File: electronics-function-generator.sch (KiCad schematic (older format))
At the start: 23 parts

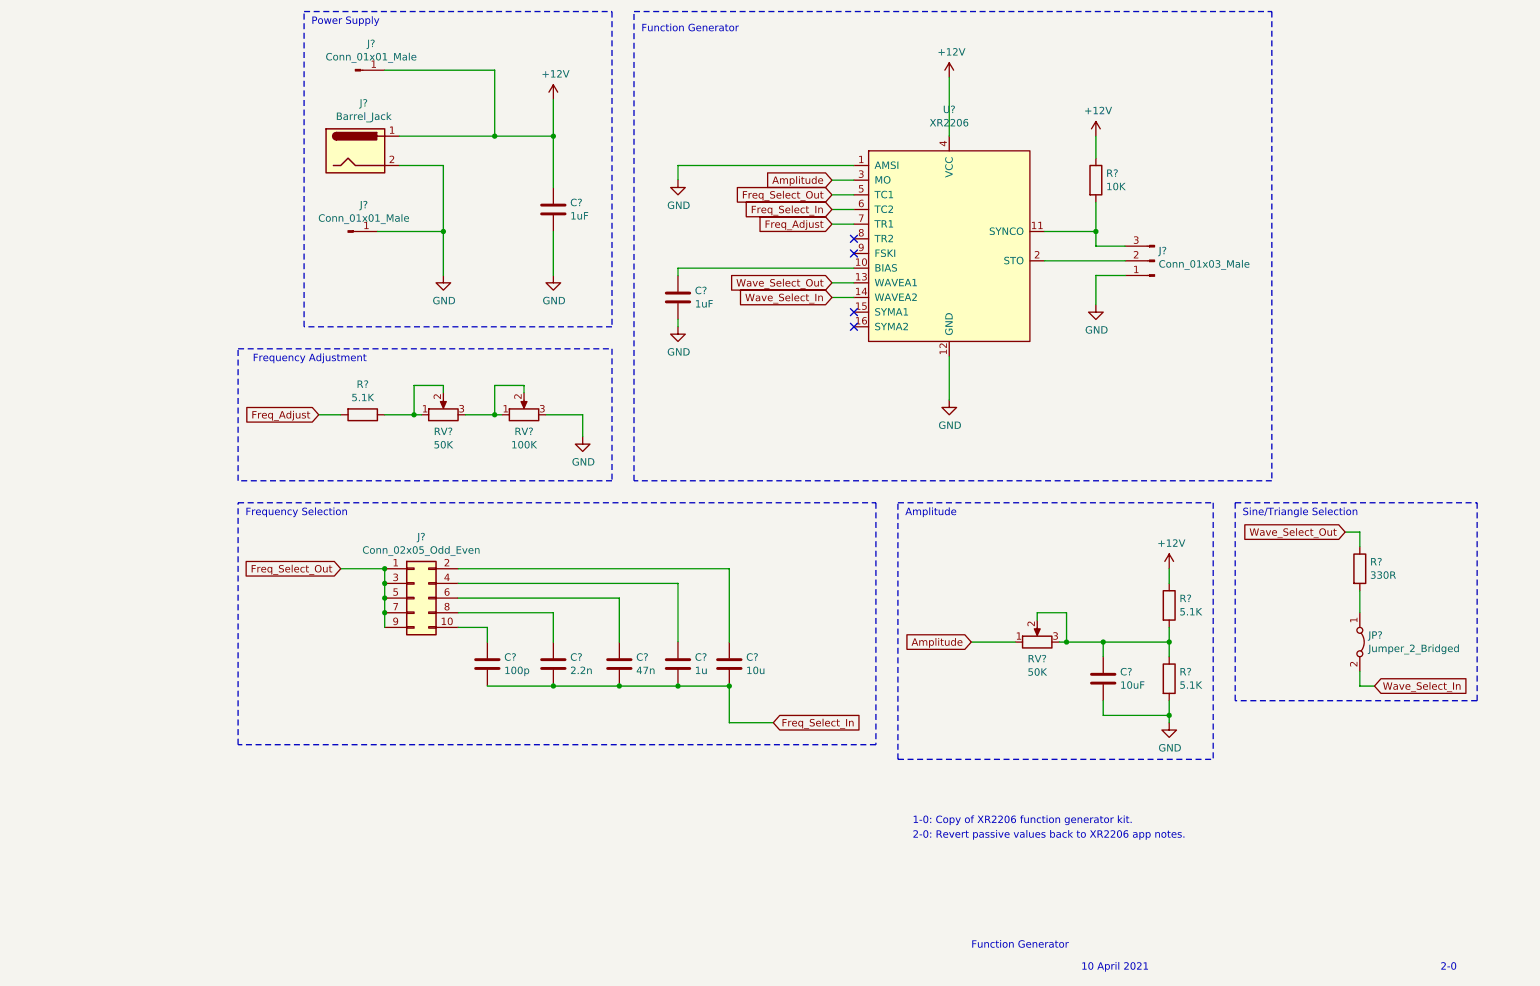
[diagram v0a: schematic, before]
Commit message: Rev 2-1: Add flexibility for harmonic balancing.
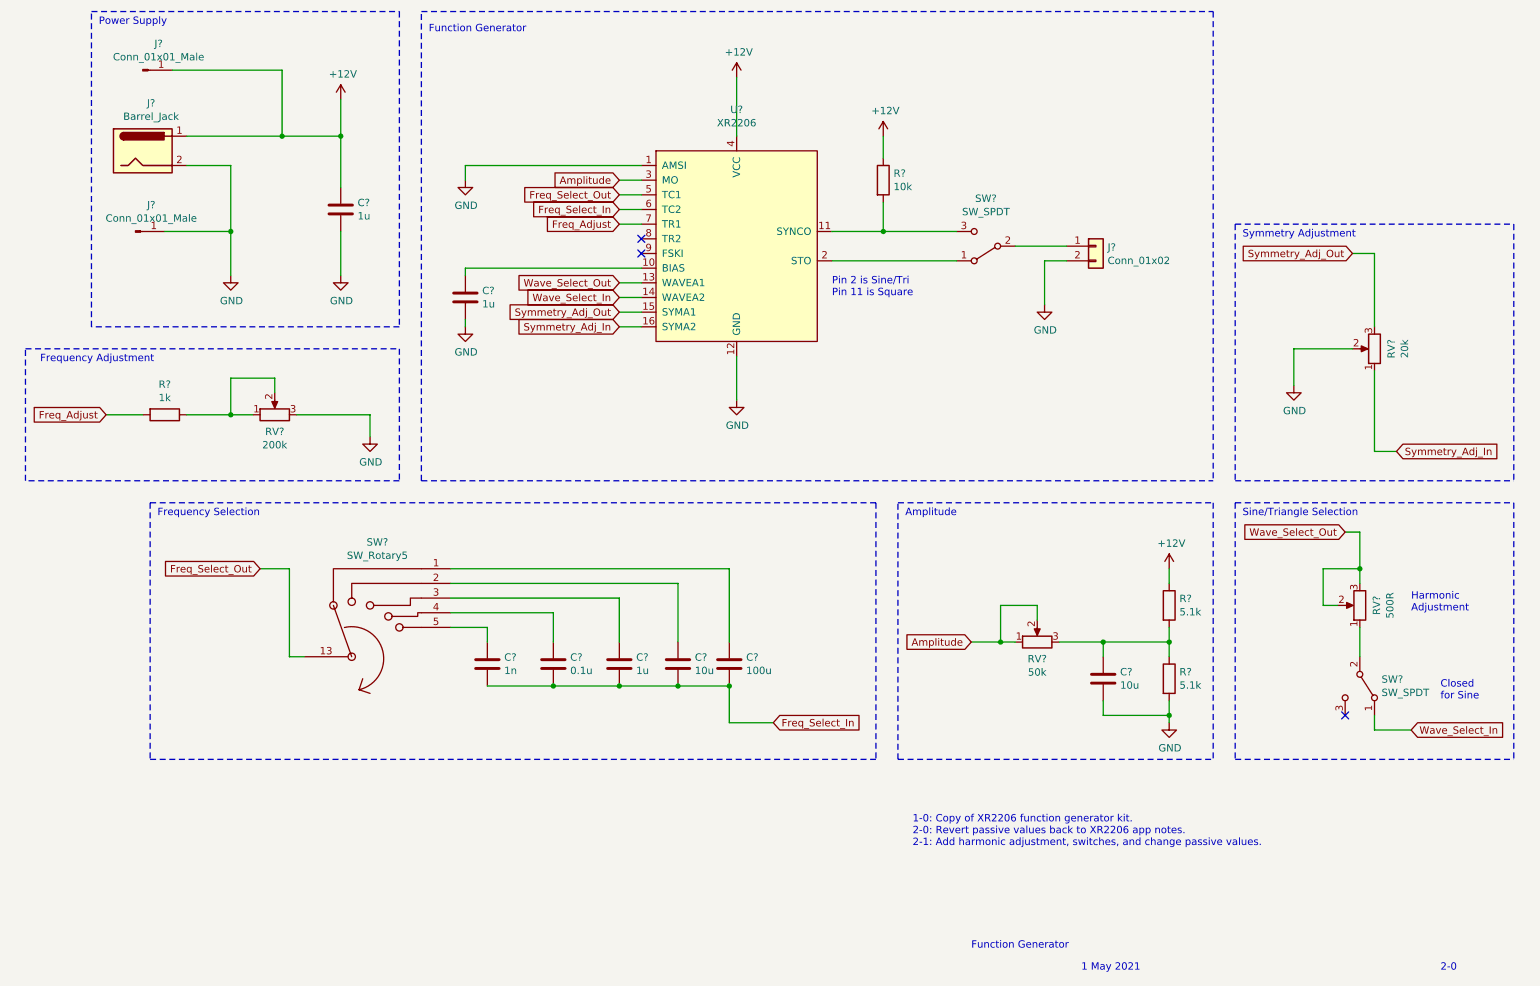
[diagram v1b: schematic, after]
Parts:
- removed J?: Conn_01x03_Male, TerminalBlock:TerminalBlock_bornier-3_P5.08mm, symbol Connector:Conn_01x03_Male
- removed J?: Conn_02x05_Odd_Even, symbol Connector_Generic:Conn_02x05_Odd_Even
- removed JP?: Jumper_2_Bridged, symbol Jumper:Jumper_2_Bridged
- removed R?: 330R, Resistor_SMD:R_1206_3216Metric_Pad1.30x1.75mm_HandSolder, symbol Device:R
- removed RV?: 100K, Potentiometer_THT:Potentiometer_Alpha_RD901F-40-00D_Single_Vertical, symbol Device:R_POT
- added J?: Conn_01x02, symbol Connector_Generic:Conn_01x02
- added RV?: 500R, Potentiometer_THT:Potentiometer_Alpha_RD901F-40-00D_Single_Vertical, symbol Device:R_POT
- added RV?: 20k, Potentiometer_THT:Potentiometer_Alpha_RD901F-40-00D_Single_Vertical, symbol Device:R_POT
- added SW? (x2): SW_SPDT, symbol Switch:SW_SPDT
- added SW?: SW_Rotary5, symbol electronics-function-generator:SW_Rotary5
- C? (x2): value 1uF -> 1u
- C?: value 10uF -> 10u
- C?: value 10u -> 100u
- C?: value 1u -> 10u
- C?: value 47n -> 1u
- C?: value 2.2n -> 0.1u
- C?: value 100p -> 1n
- R?: value 10K -> 10k
- R?: value 5.1K -> 1k
- R? (x2): value 5.1K -> 5.1k
- RV?: value 50K -> 200k
- RV?: value 50K -> 50k
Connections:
- net Amplitude: now also RV?.2
- net Freq_Select_Out: now also SW?.13
- net GND: now also RV?.3, J?.2 (Pin_2), RV?.2
- net Wave_Select_In: now also SW?.1 (A)
- net Wave_Select_Out: now also RV?.2, RV?.3
- net at R?.2, U?.11 (SYNCO): now also SW?.3 (C)
- net Symmetry_Adj_Out: now reaches U?.15 (SYMA1)
- net Symmetry_Adj_Out: now also RV?.3
- net Symmetry_Adj_In: now reaches U?.16 (SYMA2)
- net Symmetry_Adj_In: now also RV?.1
- net at U?.2 (STO): now also SW?.1 (A)
- net at C?.1, R?.1, R?.2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: no longer RV?.2
- net at C?.1: now also SW?.5
- net at C?.1: now also SW?.1
- net at C?.1: now also SW?.2
- net at C?.1: now also SW?.3
- net at C?.1: now also SW?.4
- new net: RV?.1, SW?.2 (B)
- new net: J?.1 (Pin_1), SW?.2 (B)
- no-connect marks 4 -> 3
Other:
- note added: "1 May 2021"
- note added: "1-0: Copy of XR2206 function generator kit.\n2-0: Revert passive values back to XR2206 app notes.\n2-1: Add harmonic adjustment, switches, and change passive values."
- note added: "Closed \nfor Sine"
- note added: "Harmonic \nAdjustment"
- note added: "Pin 2 is Sine/Tri\nPin 11 is Square"
- note added: "Symmetry Adjustment"
- note removed: "1-0: Copy of XR2206 function generator kit."
- note removed: "10 April 2021"
- note removed: "2-0: Revert passive values back to XR2206 app notes."
- moved on the sheet: C?, J?, R?, RV?, U?
